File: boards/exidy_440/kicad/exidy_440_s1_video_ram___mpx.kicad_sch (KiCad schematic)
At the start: 11 parts

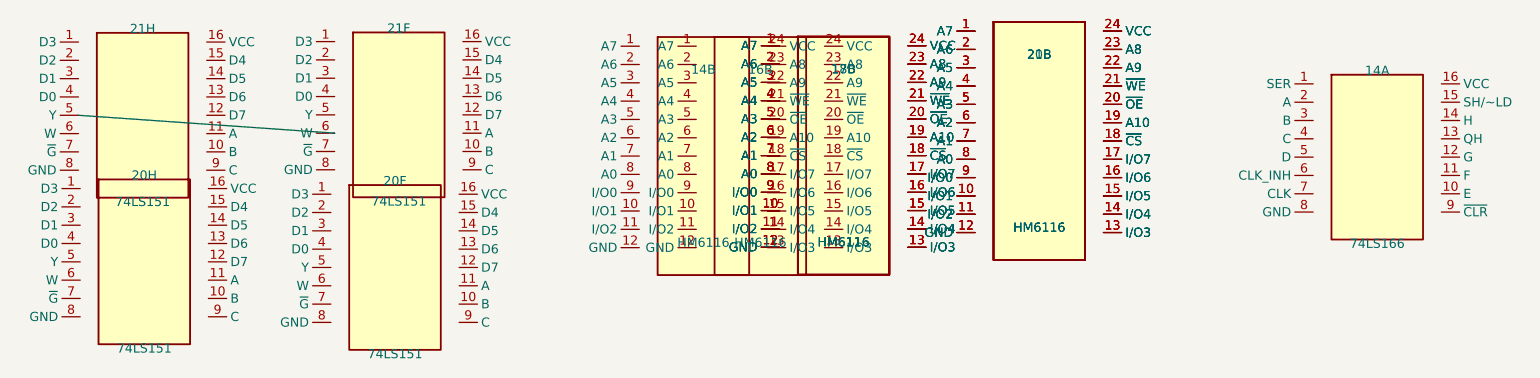
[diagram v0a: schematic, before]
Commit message: tracer: CV-assisted wire detection (v1) + import-traced-nets
New skill at .agents/skills/tracer/ with one CLI: trace. Reads a sheet
PNG and the current graph.json, emits proposed nets to JSON. Companion
import-traced-nets in graph_cli applies them with ai-source provenance.

Algorithm:
  1) Threshold (Otsu, inverted).
  2) Mask out chip bodies via component bboxes (slightly inset to keep
     pin tick-marks). Otherwise chip outlines and interior text dominate.
  3) Extract long horizontal + vertical morphological opens — schematic
     wires are axis-aligned, so this captures wires while erasing pin
     ticks (short) and text (small).
  4) Bridge right-angle turns with a 3x3 close.
  5) Connected components on the skeleton.
  6) Each pin votes for the most-common nearby skeleton label within a
     search radius. Pins sharing a label become a proposed net.

Output JSON includes label / endpoints / confidence / skeleton_area_px
per net + summary counts (skeleton_pixels, components_found,
pins_assigned). --debug writes a PNG overlay: green skeleton, blue/orange
pins (assigned vs not), gray bbox outlines.

import-traced-nets:
  - reads tracer JSON, generates unique names with --prefix (default T_)
  - assigns each endpoint sheet from the component's sheet
  - skips proposed nets with >--max-endpoints (likely bus over-connections
    or pin-position errors), default 20
  - all endpoints get edge_type=wire, evidence.source=ai with confidence
    and a note pointing back to the tracer skeleton component

Verified end-to-end on Exidy 440 sheet 1 (11 components, mostly wrong
pin_positions still at auto-DIP defaults):
  - skeleton: 957k px, 439 connected components
  - pins assigned: 203 of ~280
  - 19 proposed nets; 17 imported with --max-endpoints 10
  - validate passes; probe-list ranks them all LOW (no kind classification)
  - export-kicad: 44 wires emitted, kicad-cli sch erc rc=0

Known v1 limits documented in SKILL.md and README:
  - No junction-vs-crossing detection 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
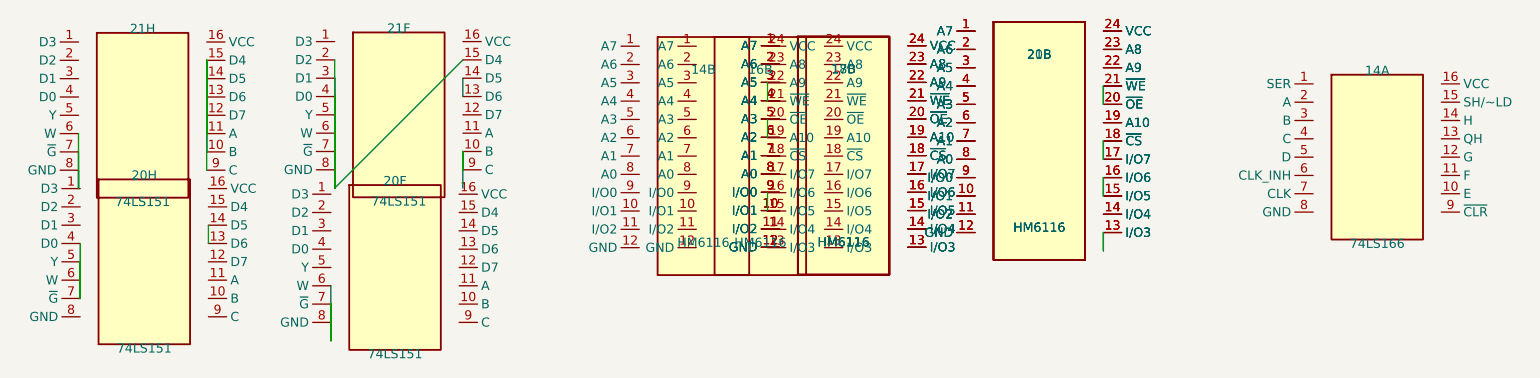
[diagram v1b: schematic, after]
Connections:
- net at 20B.15 (I/O5), 21B.15 (I/O5): now also 20B.16 (I/O6), 21B.16 (I/O6)
- net at 20B.17 (I/O7), 21B.17 (I/O7): now also 20B.18 (~{CS}), 21B.18 (~{CS})
- net at 20B.20 (~{OE}), 21B.20 (~{OE}): now also 20B.21 (~{WE}), 21B.21 (~{WE})
- net at 21H.10 (B): now also 21H.11 (A), 21H.12 (D7), 21H.13 (D6), 21H.14 (D5), 21H.15 (D4), 21H.9 (C)
- net at 14B.15 (I/O5): now also 14B.16 (I/O6)
- net at 14B.19 (A10): now also 14B.20 (~{OE})
- net at 14B.21 (~{WE}): now also 14B.22 (A9)
- net at 21F.10 (B): now also 21F.9 (C)
- net at 21F.13 (D6): now also 21F.14 (D5)
- net at 21F.15 (D4): now also 21F.2 (D2), 21F.3 (D1), 21F.4 (D0), 21F.5 (Y), 21F.6 (W), 21F.7 (~{G}), 21F.8 (GND)
- net at 20F.6 (W): now also 20F.7 (~{G}), 20F.8 (GND)
- net at 20H.13 (D6): now also 20H.14 (D5)
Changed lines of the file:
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@@
     )
   )
-  (wire (pts (xy 91.4663 76.7559) (xy 127 79.237))
+  (wire (pts (xy 144.78 81.777) (xy 144.78 84.317))
     (stroke (width 0) (type default))
   )
+  (wire (pts (xy 144.78 81.777) (xy 144.78 86.857))
+    (stroke (width 0) (type default))
+  )
+  (wire (pts (xy 127 86.857) (xy 127 84.317))
+    (stroke (width 0) (type default))
+  )
+  (wire (pts (xy 127 86.857) (xy 127 81.777))
+    (stroke (width 0) (type default))
+  )
+  (wire (pts (xy 127 86.857) (xy 127 79.237))
+    (stroke (width 0) (type default))
+  )
+  (wire (pts (xy 127 86.857) (xy 127 76.697))
+    (stroke (width 0) (type default))
+  )
+  (wire (pts (xy 127 86.857) (xy 127 74.157))
+    (stroke (width 0) (type default))
+  )
+  (wire (pts (xy 127 86.857) (xy 127 71.617))
+    (stroke (width 0) (type default))
+  )
+  (wire (pts (xy 127 86.857) (xy 127 69.077))
+    (stroke (width 0) (type default))
+  )
+  (wire (pts (xy 127 86.857) (xy 144.78 69.077))
+    (stroke (width 0) (type default))
+  )
+  (wire (pts (xy 91.4663 86.9159) (xy 91.4663 84.3759))
+    (stroke (width 0) (type default))
+  )
+  (wire (pts (xy 91.4663 86.9159) (xy 91.4663 81.8359))
+    (stroke (width 0) (type default))
+  )
+  (wire (pts (xy 91.4663 86.9159) (xy 91.4663 79.2959))
+    (stroke (width 0) (type default))
+  )
+  (wire (pts (xy 109.246 69.1359) (xy 109.246 71.6759))
+    (stroke (width 0) (type default))
+  )
+  (wire (pts (xy 109.246 69.1359) (xy 109.246 74.2159))
+    (stroke (width 0) (type default))
+  )
+  (wire (pts (xy 109.246 69.1359) (xy 109.246 76.7559))
+    (stroke (width 0) (type default))
+  )
+  (wire (pts (xy 109.246 69.1359) (xy 109.246 79.2959))
+    (stroke (width 0) (type default))
+  )
+  (wire (pts (xy 109.246 69.1359) (xy 109.246 81.8359))
+    (stroke (width 0) (type default))
+  )
+  (wire (pts (xy 109.246 69.1359) (xy 109.246 84.3759))
+    (stroke (width 0) (type default))
+  )
+  (wire (pts (xy 233.613 93.021) (xy 233.613 95.561))
+    (stroke (width 0) (type default))
+  )
+  (wire (pts (xy 233.613 93.021) (xy 233.613 93.021))
+    (stroke (width 0) (type default))
+  )
+  (wire (pts (xy 233.613 93.021) (xy 233.613 95.561))
+    (stroke (width 0) (type default))
+  )
+  (wire (pts (xy 233.613 90.481) (xy 233.613 90.481))
+    (stroke (width 0) (type default))
+  )
+  (wire (pts (xy 187.03 87.4929) (xy 187.03 90.0329))
+    (stroke (width 0) (type default))
+  )
+  (wire (pts (xy 233.613 85.401) (xy 233.613 87.941))
+    (stroke (width 0) (type default))
+  )
+  (wire (pts (xy 233.613 85.401) (xy 233.613 85.401))
+    (stroke (width 0) (type default))
+  )
+  (wire (pts (xy 233.613 85.401) (xy 233.613 87.941))
+    (stroke (width 0) (type default))
+  )
+  (wire (pts (xy 233.613 80.321) (xy 233.613 82.861))
+    (stroke (width 0) (type default))
+  )
+  (wire (pts (xy 233.613 80.321) (xy 233.613 80.321))
+    (stroke (width 0) (type default))
+  )
+  (wire (pts (xy 233.613 80.321) (xy 233.613 82.861))
+    (stroke (width 0) (type default))
+  )
+  (wire (pts (xy 144.78 71.617) (xy 144.78 74.157))
+    (stroke (width 0) (type default))
+  )
+  (wire (pts (xy 233.613 77.781) (xy 233.613 77.781))
+    (stroke (width 0) (type default))
+  )
+  (wire (pts (xy 91.6997 102.163) (xy 91.6997 99.6231))
+    (stroke (width 0) (type default))
+  )
+  (wire (pts (xy 91.6997 102.163) (xy 91.6997 97.0831))
+    (stroke (width 0) (type default))
+  )
+  (wire (pts (xy 91.6997 102.163) (xy 91.6997 94.5431))
+    (stroke (width 0) (type default))
+  )
+  (wire (pts (xy 126.474 108.024) (xy 126.474 105.484))
+    (stroke (width 0) (type default))
+  )
+  (wire (pts (xy 126.474 108.024) (xy 126.474 102.944))
+    (stroke (width 0) (type default))
+  )
+  (wire (pts (xy 126.474 108.024) (xy 126.474 100.404))
+    (stroke (width 0) (type default))
+  )
+  (wire (pts (xy 233.613 72.701) (xy 233.613 75.241))
+    (stroke (width 0) (type default))
+  )
+  (wire (pts (xy 233.613 72.701) (xy 233.613 72.701))
+    (stroke (width 0) (type default))
+  )
+  (wire (pts (xy 233.613 72.701) (xy 233.613 75.241))
+    (stroke (width 0) (type default))
+  )
+  (wire (pts (xy 187.03 77.3329) (xy 187.03 79.8729))
+    (stroke (width 0) (type default))
+  )
+  (wire (pts (xy 187.03 72.2529) (xy 187.03 74.7929))
+    (stroke (width 0) (type default))
+  )
+  (wire (pts (xy 109.48 92.0031) (xy 109.48 94.5431))
+    (stroke (width 0) (type default))
+  )
